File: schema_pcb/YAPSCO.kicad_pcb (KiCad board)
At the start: 2 copper layers, 82.8 x 73.2 mm, 80 parts, among them J1 DB15_Female, J2 DB9_Female_MountingHoles, K1 Supply, K3 FautlPol, P1 STEP, P2 DIR, P3 CONN, P4 ENABLE, P5 +-10V, P6 InOut, P7 Jumper, P8 Jumper, P9 Jumper, Q1 NPN, U1 7805, U10 MC33063AD, U2 dsPIC30F4012, U3 6N137, U4 6N137, U5 6N137, U6 LM358, U7 74HC14, U8 LM339D, U9 L7812

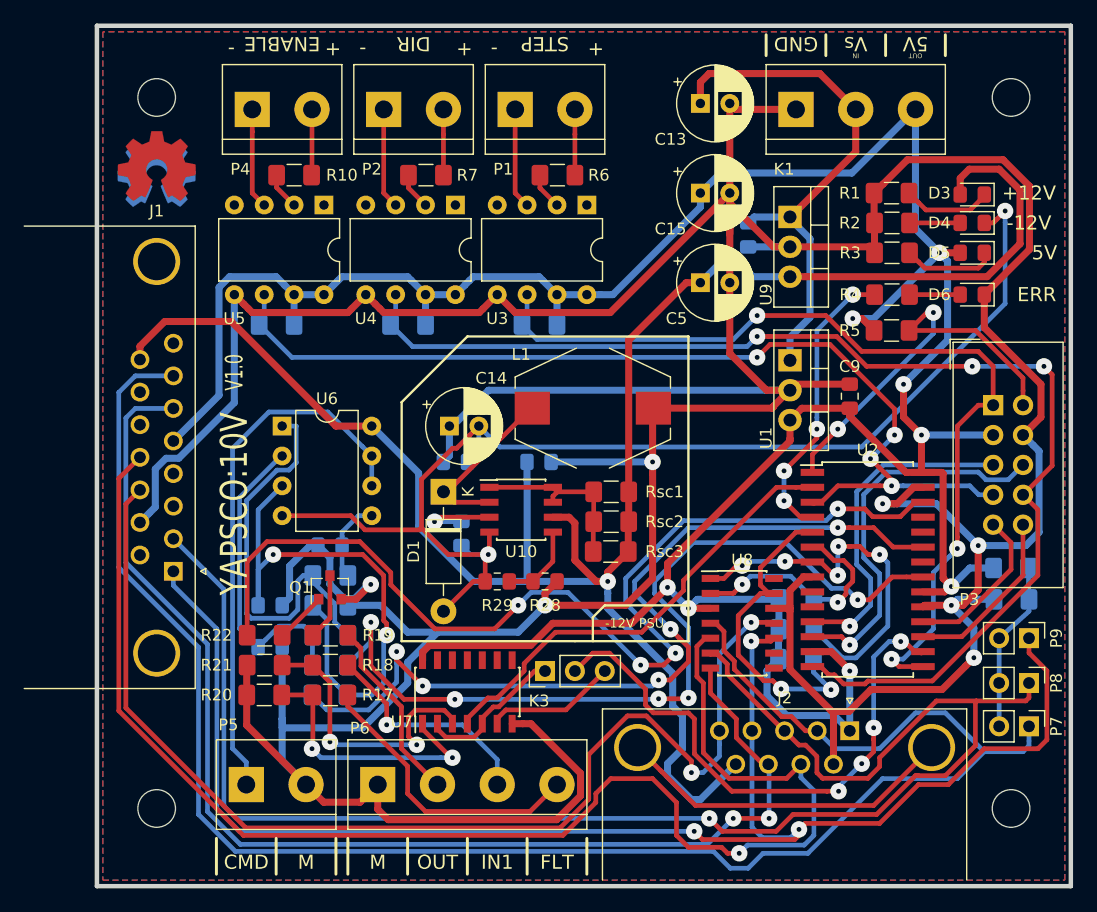
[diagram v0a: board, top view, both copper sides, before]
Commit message: Feedback changed to cheap linear scale
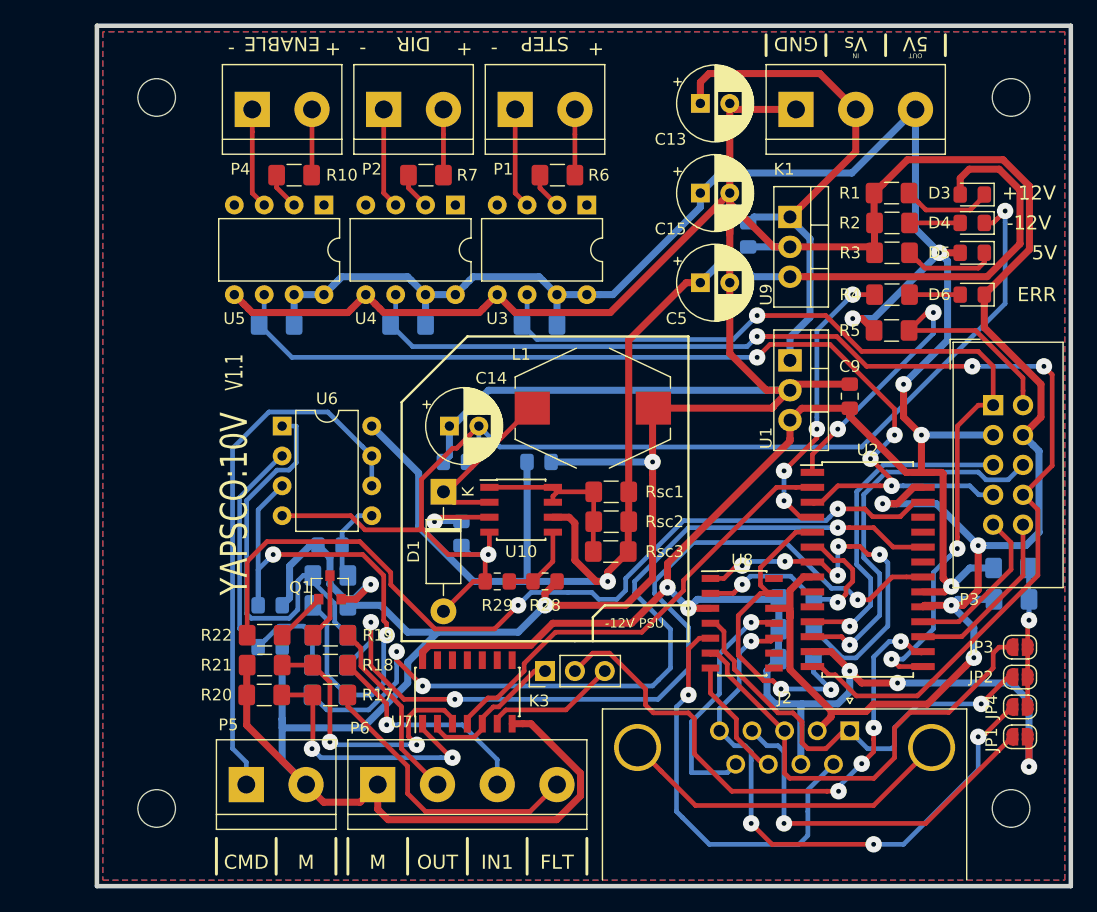
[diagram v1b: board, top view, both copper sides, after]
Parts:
- removed J1: DB15_Female, Connector_Dsub:DSUB-15_Female_Horizontal_P2.77x2.84mm_EdgePinOffset9.90mm_Housed_MountingHolesOffset11.32mm
- removed P7, P8, P9: Jumper, Connector_PinHeader_2.54mm:PinHeader_1x02_P2.54mm_Vertical
- removed REF** (x2): OSHW-Symbol_6.7x6mm_Copper, Symbol:OSHW-Symbol_6.7x6mm_Copper
- added JP1: SolderJumper_2_Open, Jumper:SolderJumper-2_P1.3mm_Open_RoundedPad1.0x1.5mm, F.Cu at (190.2, 128.5)
- added JP2: SolderJumper_2_Open, Jumper:SolderJumper-2_P1.3mm_Open_RoundedPad1.0x1.5mm, F.Cu at (190.2, 123.4)
- added JP3: SolderJumper_2_Open, Jumper:SolderJumper-2_P1.3mm_Open_RoundedPad1.0x1.5mm, F.Cu at (190.2, 120.9)
- added JP4: SolderJumper_2_Open, Jumper:SolderJumper-2_P1.3mm_Open_RoundedPad1.0x1.5mm, F.Cu at (190.2, 126.0)
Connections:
- J2 pad 1: +5V -> /Encoder/A-
- J2 pad 2: /Encoder/A- -> GND
- J2 pad 4: /Encoder/I- -> Net-(J2-Pad4)
- J2 pad 5: /Encoder/I+ -> /Encoder/I-
- J2 pad 6: GND -> /Encoder/A+
- J2 pad 7: /Encoder/A+ -> +5V
- J2 pad 9: +12V -> /Encoder/I+
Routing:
- net /Encoder/A-: track 154.1 -> 37.2 mm, vias 0 -> 1
- net /Encoder/B+: track 105.6 -> 10.6 mm, vias 2 -> 0
- net /Encoder/B-: track 133.5 -> 39.6 mm, vias 1 -> 0
- net /Encoder/A+: track 120.0 -> 36.5 mm
- net /Encoder/I-: track 129.0 -> 50.2 mm, vias 3 -> 4
- net /Encoder/I+: track 97.5 -> 20.9 mm, vias 2 -> 1
- net +12V: track 171.0 -> 118.0 mm
- net Net-(J2-Pad4): track 0.00 -> 32.0 mm, vias 0 -> 1
- net GND: track 459.2 -> 434.0 mm
- net /InterfaceDriver/OUT1: track 87.9 -> 74.2 mm, vias 4 -> 2
- net +5V: track 259.8 -> 263.5 mm, vias 8 -> 10
- net +2V5: track 14.6 -> 12.2 mm, vias 0 -> 1
- net /dsPIC/PWM_H_A: track 74.4 -> 72.6 mm, vias 5 -> 3
- net /InterfaceDriver/Neg: track 74.5 -> 73.1 mm, vias 5 -> 3
- net /MotionControllerInput/DIR: track 103.7 -> 104.5 mm
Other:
- board text added: "V1.1"
- board text removed: "V1.0"
